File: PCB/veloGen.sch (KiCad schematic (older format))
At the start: 42 parts, among them J1 progButton, J2 Gen. IN, J3 Batt, P1 TTL_232R_3V3, P2 CONN_01X04, Q1 STL4P3LLH6, Q2 BSS138_ok, U1 ESP-WROOM-32, U2 TS1101, U3 TS1101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

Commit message: Added SEPIC ltspice model
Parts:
- gave numbers to parts that had none: 6
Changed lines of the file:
@@
 $EndComp
 $Comp
-L GND #PWR12
+L GND #PWR15
 U 1 1 58CDDA95
 P 6550 3600
-F 0 "#PWR12" H 6550 3350 50  0001 C CNN
+F 0 "#PWR15" H 6550 3350 50  0001 C CNN
 F 1 "GND" H 6555 3427 50  0000 C CNN
 F 2 "" H 6550 3600 50  0001 C CNN
@@
 NoConn ~ 10300 2600
 $Comp
-L +3V3 #PWR19
+L +3V3 #PWR22
 U 1 1 58CDF05C
 P 10600 2500
-F 0 "#PWR19" H 10600 2350 50  0001 C CNN
+F 0 "#PWR22" H 10600 2350 50  0001 C CNN
 F 1 "+3V3" H 10615 2673 50  0000 C CNN
 F 2 "" H 10600 2500 50  0001 C CNN
@@
 $EndComp
 $Comp
-L +BATT #PWR11
+L +BATT #PWR14
 U 1 1 58D0C801
 P 6550 2450
-F 0 "#PWR11" H 6550 2300 50  0001 C CNN
+F 0 "#PWR14" H 6550 2300 50  0001 C CNN
 F 1 "+BATT" H 6700 2550 50  0000 C CNN
 F 2 "" H 6550 2450 50  0001 C CNN
@@
 $EndComp
 $Comp
-L +3V3 #PWR13
+L +3V3 #PWR16
 U 1 1 58D133CF
 P 7050 2800
-F 0 "#PWR13" H 7050 2650 50  0001 C CNN
+F 0 "#PWR16" H 7050 2650 50  0001 C CNN
 F 1 "+3V3" V 7050 3050 50  0000 C CNN
 F 2 "" H 7050 2800 50  0001 C CNN
@@
 $EndComp
 $Comp
-L GND #PWR14
+L GND #PWR17
 U 1 1 58D1409D
 P 8050 2700
-F 0 "#PWR14" H 8050 2450 50  0001 C CNN
+F 0 "#PWR17" H 8050 2450 50  0001 C CNN
 F 1 "GND" V 8150 2650 50  0000 C CNN
 F 2 "" H 8050 2700 50  0001 C CNN
@@
 $EndComp
 $Comp
-L +3V3 #PWR5
+L +3V3 #PWR7
 U 1 1 58D16995
 P 3750 1250
-F 0 "#PWR5" H 3750 1100 50  0001 C CNN
+F 0 "#PWR7" H 3750 1100 50  0001 C CNN
 F 1 "+3V3" V 3750 1500 50  0000 C CNN
 F 2 "" H 3750 1250 50  0001 C CNN
@@
 $EndComp
 $Comp
-L GND #PWR7
+L GND #PWR9
 U 1 1 58D169A5
 P 4750 1150
-F 0 "#PWR7" H 4750 900 50  0001 C CNN
+F 0 "#PWR9" H 4750 900 50  0001 C CNN
 F 1 "GND" V 4750 950 50  0000 C CNN
 F 2 "" H 4750 1150 50  0001 C CNN
@@
 Igen
 $Comp
-L GND #PWR6
+L GND #PWR8
 U 1 1 58D1723C
 P 3800 1800
-F 0 "#PWR6" H 3800 1550 50  0001 C CNN
+F 0 "#PWR8" H 3800 1550 50  0001 C CNN
 F 1 "GND" H 3805 1627 50  0000 C CNN
 F 2 "" H 3800 1800 50  0001 C CNN
@@
 $EndComp
 $Comp
-L GND #PWR8
+L GND #PWR10
 U 1 1 58D18FFC
 P 4800 1800
-F 0 "#PWR8" H 4800 1550 50  0001 C CNN
+F 0 "#PWR10" H 4800 1550 50  0001 C CNN
 F 1 "GND" H 4805 1627 50  0000 C CNN
 F 2 "" H 4800 1800 50  0001 C CNN
@@
 buckPwm
 $Comp
-L +3V3 #PWR2
+L +3V3 #PWR4
 U 1 1 58D24DE5
 P 2550 5050
-F 0 "#PWR2" H 2550 4900 50  0001 C CNN
+F 0 "#PWR4" H 2550 4900 50  0001 C CNN
 F 1 "+3V3" H 2550 5200 50  0000 C CNN
 F 2 "" H 2550 5050 50  0001 C CNN
@@
 $EndComp
 $Comp
-L GND #PWR3
+L GND #PWR5
 U 1 1 58D25BFF
 P 2950 5100
-F 0 "#PWR3" H 2950 4850 50  0001 C CNN
+F 0 "#PWR5" H 2950 4850 50  0001 C CNN
 F 1 "GND" H 2950 5150 50  0000 C CNN
 F 2 "" H 2950 5100 50  0001 C CNN
@@
 $EndComp
 $Comp
-L GND #PWR9
+L GND #PWR12
 U 1 1 58D26A6B
 P 5050 5000
-F 0 "#PWR9" H 5050 4750 50  0001 C CNN
+F 0 "#PWR12" H 5050 4750 50  0001 C CNN
 F 1 "GND" H 5050 5050 50  0000 C CNN
 F 2 "" H 5050 5000 50  0001 C CNN
@@
 $EndComp
 $Comp
-L GND #PWR18
+L GND #PWR21
 U 1 1 58D236E7
 P 9950 4600
-F 0 "#PWR18" H 9950 4350 50  0001 C CNN
+F 0 "#PWR21" H 9950 4350 50  0001 C CNN
 F 1 "GND" H 9955 4427 50  0000 C CNN
 F 2 "" H 9950 4600 50  0001 C CNN
@@
 $EndComp
 $Comp
-L GND #PWR15
+L GND #PWR18
 U 1 1 58D25A85
 P 8750 5350
-F 0 "#PWR15" H 8750 5100 50  0001 C CNN
+F 0 "#PWR18" H 8750 5100 50  0001 C CNN
 F 1 "GND" V 8750 5150 50  0000 C CNN
 F 2 "" H 8750 5350 50  0001 C CNN
@@
 $EndComp
 $Comp
-L +3V3 #PWR16
+L +3V3 #PWR19
 U 1 1 58D1F535
 P 9100 4800
-F 0 "#PWR16" H 9100 4650 50  0001 C CNN
+F 0 "#PWR19" H 9100 4650 50  0001 C CNN
 F 1 "+3V3" H 9250 4850 50  0000 C CNN
 F 2 "" H 9100 4800 50  0001 C CNN
@@
 $EndComp
 $Comp
-L +3V3 #PWR17
+L +3V3 #PWR20
 U 1 1 58D1FFAD
 P 9300 5750
-F 0 "#PWR17" H 9300 5600 50  0001 C CNN
+F 0 "#PWR20" H 9300 5600 50  0001 C CNN
 F 1 "+3V3" H 9450 5800 50  0000 C CNN
 F 2 "" H 9300 5750 50  0001 C CNN
@@
 rstBtn
 $Comp
-L GND #PWR4
+L GND #PWR6
 U 1 1 58D25783
 P 3550 6800
-F 0 "#PWR4" H 3550 6550 50  0001 C CNN
+F 0 "#PWR6" H 3550 6550 50  0001 C CNN
 F 1 "GND" H 3400 6750 50  0000 C CNN
 F 2 "" H 3550 6800 50  0001 C CNN
@@
 $EndComp
 $Comp
-L GND #PWR10
+L GND #PWR13
 U 1 1 58D266BB
 P 5850 5850
-F 0 "#PWR10" H 5850 5600 50  0001 C CNN
+F 0 "#PWR13" H 5850 5600 50  0001 C CNN
 F 1 "GND" H 6150 5750 50  0000 C CNN
 F 2 "" H 5850 5850 50  0001 C CNN
@@
 NoConn ~ 5850 5700
 $Comp
-L GND #PWR1
+L GND #PWR11
 U 1 1 58D2F2FA
 P 4800 6750
-F 0 "#PWR1" H 4800 6500 50  0001 C CNN
+F 0 "#PWR11" H 4800 6500 50  0001 C CNN
 F 1 "GND" H 4850 6850 50  0000 C CNN
 F 2 "" H 4800 6750 50  0001 C CNN
@@
 $EndComp
 $Comp
-L R R?
+L R R14
 U 1 1 58E35502
 P 2200 6400
-F 0 "R?" V 1993 6400 50  0000 C CNN
+F 0 "R14" V 1993 6400 50  0000 C CNN
 F 1 "470R" V 2084 6400 50  0000 C CNN
 F 2 "" V 2130 6400 50  0001 C CNN
@@
 NoConn ~ 4900 5300
 $Comp
-L D_Zener D?
+L D_Zener D7
 U 1 1 58E3687C
 P 4050 3000
-F 0 "D?" V 4004 3079 50  0000 L CNN
+F 0 "D7" V 4004 3079 50  0000 L CNN
 F 1 "30V, 3W" V 4095 3079 50  0000 L CNN
 F 2 "" H 4050 3000 50  0001 C CNN
@@
 	8800 5150 8800 4300
 $Comp
-L Crystal Y?
+L Crystal Y1
 U 1 1 58E37985
 P 2200 5950
-F 0 "Y?" V 2000 5850 50  0000 L CNN
+F 0 "Y1" V 2000 5850 50  0000 L CNN
 F 1 "32.768 kHz" V 1900 5750 50  0000 L CNN
 F 2 "" H 2200 5950 50  0001 C CNN
@@
 	2400 5900 2400 6100
 $Comp
-L C C?
+L C C9
 U 1 1 58E3A322
 P 1850 5800
-F 0 "C?" V 1800 5700 50  0000 C CNN
+F 0 "C9" V 1800 5700 50  0000 C CNN
 F 1 "12pF" V 1689 5800 50  0000 C CNN
 F 2 "" H 1888 5650 50  0001 C CNN
@@
 $EndComp
 $Comp
-L C C?
+L C C12
 U 1 1 58E3A3E7
 P 1850 6100
-F 0 "C?" V 1900 6200 50  0000 C CNN
+F 0 "C12" V 1900 6200 50  0000 C CNN
 F 1 "12pF" V 1700 6100 50  0000 C CNN
 F 2 "" H 1888 5950 50  0001 C CNN
@@
 Connection ~ 2200 6100
 $Comp
-L GND #PWR?
+L GND #PWR3
 U 1 1 58E3C87D
 P 1650 6400
-F 0 "#PWR?" H 1650 6150 50  0001 C CNN
+F 0 "#PWR3" H 1650 6150 50  0001 C CNN
 F 1 "GND" V 1650 6200 50  0000 C CNN
 F 2 "" H 1650 6400 50  0001 C CNN
@@
 $EndComp
 $Comp
-L LED D?
+L LED D5
 U 1 1 58E350A9
 P 1850 6400
-F 0 "D?" H 2000 6300 50  0000 C CNN
+F 0 "D5" H 2000 6300 50  0000 C CNN
 F 1 "LED" H 1850 6300 50  0000 C CNN
 F 2 "LEDs:LED_0805" H 1850 6400 50  0001 C CNN
@@
 	2050 6400 2000 6400
 $Comp
-L GND #PWR?
+L GND #PWR2
 U 1 1 58E3DA98
 P 1650 6100
-F 0 "#PWR?" H 1650 5850 50  0001 C CNN
+F 0 "#PWR2" H 1650 5850 50  0001 C CNN
 F 1 "GND" V 1650 5900 50  0000 C CNN
 F 2 "" H 1650 6100 50  0001 C CNN
@@
 $EndComp
 $Comp
-L GND #PWR?
+L GND #PWR1
 U 1 1 58E3DB09
 P 1650 5800
-F 0 "#PWR?" H 1650 5550 50  0001 C CNN
+F 0 "#PWR1" H 1650 5550 50  0001 C CNN
 F 1 "GND" V 1650 5600 50  0000 C CNN
 F 2 "" H 1650 5800 50  0001 C CNN

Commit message: Schematic work
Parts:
- R3, R8: value R050 -> R010
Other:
- note added: "Gain = 100 x\n1 V / A"
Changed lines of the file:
@@
 P 3300 2500
 F 0 "R3" H 3370 2546 50  0000 L CNN
-F 1 "R050" H 3370 2455 50  0000 L CNN
+F 1 "R010" H 3370 2455 50  0000 L CNN
 F 2 "Resistors_SMD:R_0805" V 3230 2500 50  0001 C CNN
 F 3 "" H 3300 2500 50  0001 C CNN
@@
 P 6550 2800
 F 0 "R8" H 6620 2846 50  0000 L CNN
-F 1 "R050" H 6620 2755 50  0000 L CNN
+F 1 "R010" H 6620 2755 50  0000 L CNN
 F 2 "Resistors_SMD:R_0805" V 6480 2800 50  0001 C CNN
 F 3 "" H 6550 2800 50  0001 C CNN
@@
 Wire Wire Line
 	4800 6700 4800 6750
+Text Notes 4050 1950 0    60   ~ 0
+Gain = 100 x\n1 V / A
+Text Notes 7350 2350 0    60   ~ 0
+Gain = 100 x\n1 V / A
 $EndSCHEMATC

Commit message: Simplified schematic and started layout
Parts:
- removed C12, C9: 12pF, symbol C
- removed C3, C6: 470n, Capacitors_SMD:C_0805, symbol C
- removed C4, C7: 47n, Capacitors_SMD:C_0805, symbol C
- removed D7: 30V, 3W, symbol D_Zener
- removed J1: progButton, Pin_Headers:Pin_Header_Straight_1x02_Pitch2.54mm, symbol CONN_01X02
- removed R3, R8: R010, Resistors_SMD:R_0805, symbol R
- removed U2, U3: TS1101, TO_SOT_Packages_SMD:SOT-23-6_Handsoldering, symbol TS1101
- removed Y1: 32.768 kHz, symbol Crystal
- added U2: PROG, myStuff:EVQQ2, symbol TACTILE
- J3: value Batt -> Bat
- R14: footprint (none) -> Resistors_SMD:R_0805
- U4: footprint TO_SOT_Packages_SMD:SOT-23-6_Handsoldering -> TO_SOT_Packages_SMD:SOT-23-6
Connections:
- net labels added: sepicImax, sepicPwm
- net labels removed: Ibatt, IbattSign, Igen, buckPwm
- wire segments 134 -> 94
- no-connect marks 20 -> 25
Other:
- note removed: "Gain = 100 x\n1 V / A"
- moved on the sheet: C5, R6, R7

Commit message: completed an ugly pcb with minimalistic fuctionality
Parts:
- removed P1: TTL_232R_3V3, Pin_Headers:Pin_Header_Straight_1x06_Pitch2.54mm, symbol TTL_232R_3V3
- removed P2: CONN_01X04, Pin_Headers:Pin_Header_Straight_1x04_Pitch2.54mm, symbol CONN_01X04
- removed Q1: STL4P3LLH6, myStuff:PowerFLAT_2x2, symbol STL4P3LLH6
- removed Q2: BSS138_ok, TO_SOT_Packages_SMD:SOT-23, symbol BSS138_ok
- removed R10, R9: 200R, Resistors_SMD:R_0805, symbol R
- removed R11, R12: 4k7, Resistors_SMD:R_0805, symbol R
- removed R13: 4.7Meg, Resistors_SMD:R_0805, symbol R
- removed U2: PROG, myStuff:EVQQ2, symbol TACTILE
- added J1: Conn_01x06, myStuff:myPogoPads, symbol Conn_01x06
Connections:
- net labels added: progFlag
- wire segments 94 -> 75
- no-connect marks 25 -> 21
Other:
- note added: "5 V"
- note added: "GND"
- note added: "RXD"
- note added: "Rst"
- note added: "TXD"

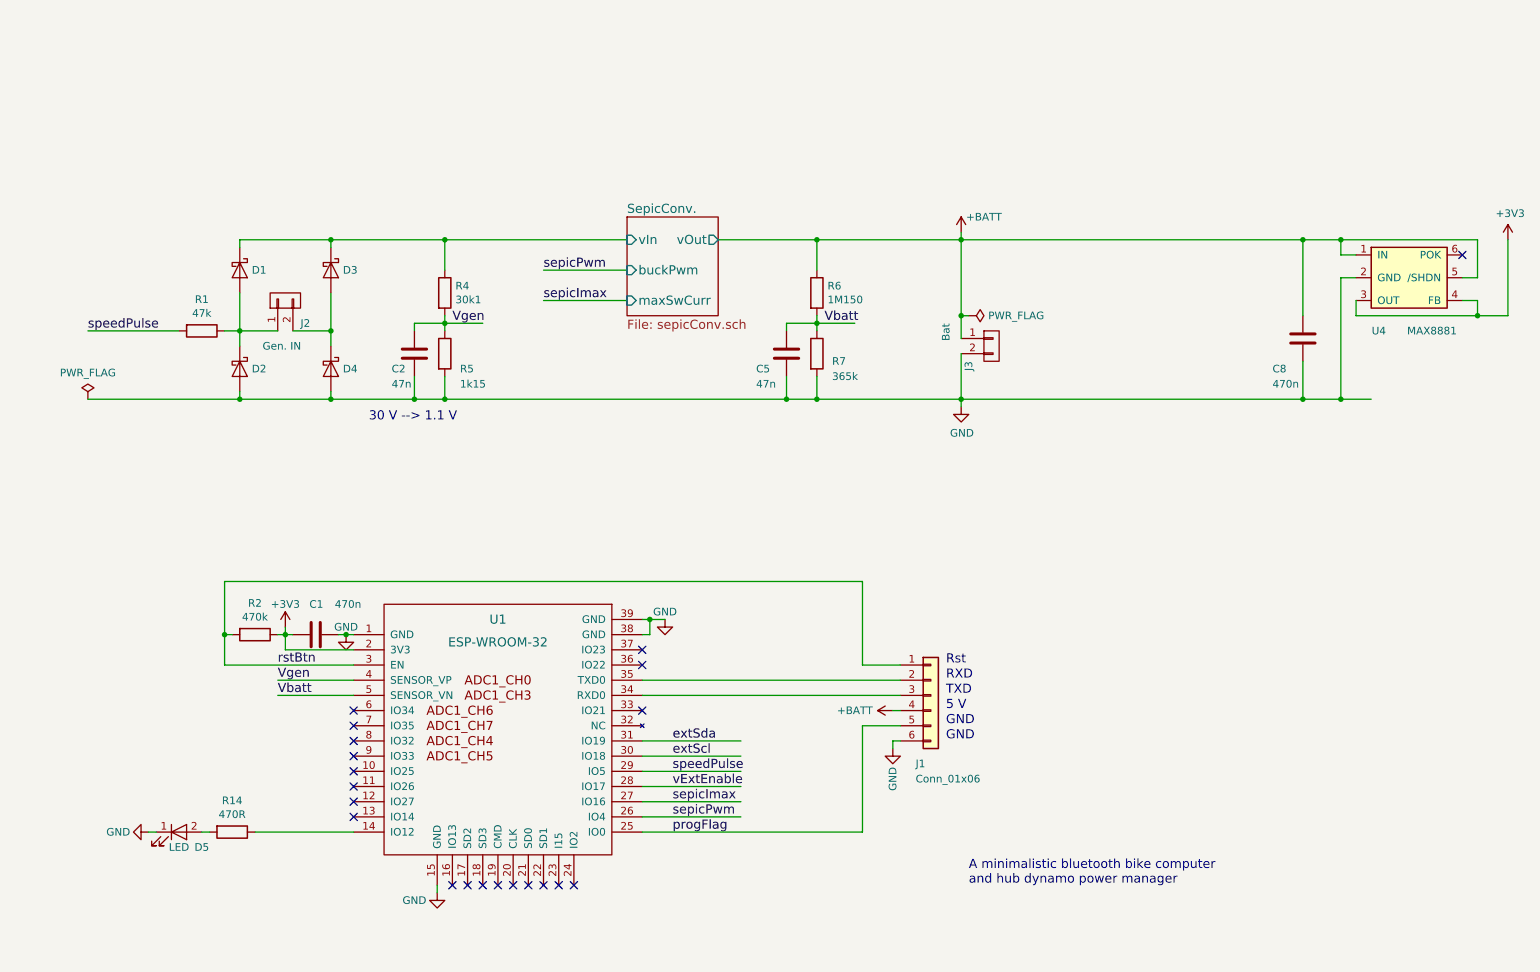
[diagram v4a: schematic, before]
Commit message: Added batery current sense
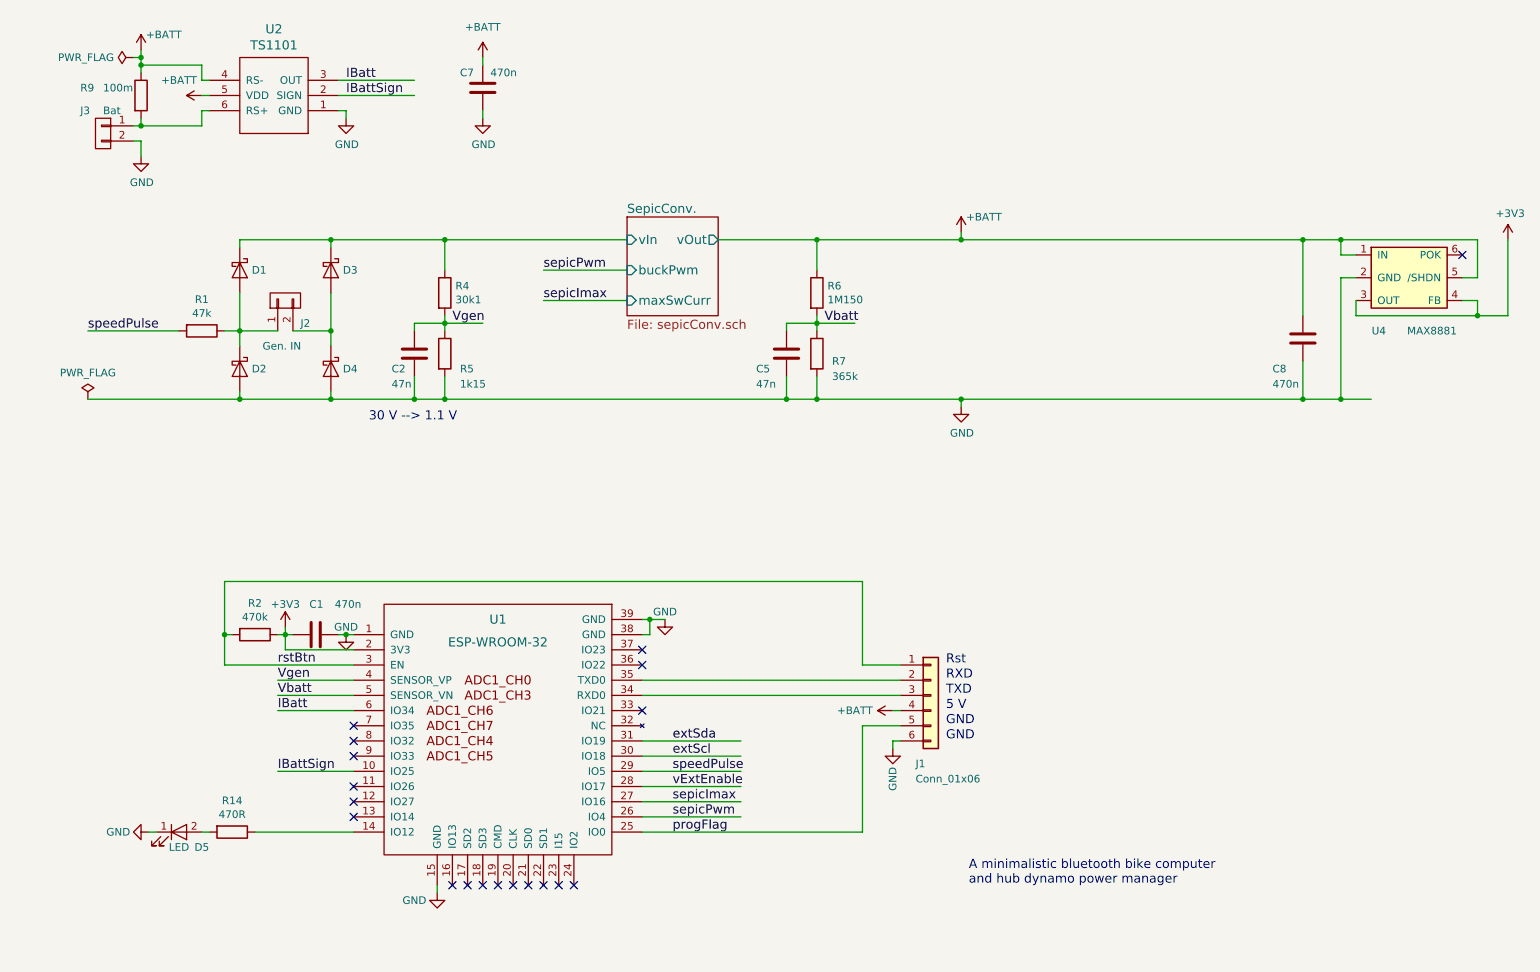
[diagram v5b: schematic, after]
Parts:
- added C7: 470n, Capacitors_SMD:C_0805, symbol C
- added R9: 100m, Resistors_SMD:R_1206, symbol R
- added U2: TS1101, TO_SOT_Packages_SMD:SOT-23-6_Handsoldering, symbol TS1101
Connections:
- net labels added: IBatt, IBattSign
- wire segments 75 -> 94
- no-connect marks 21 -> 19
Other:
- moved on the sheet: J3
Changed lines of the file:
@@
-EESchema Schematic File Version 2
+EESchema Schematic File Version 3
 LIBS:veloGen-rescue
 LIBS:power
@@
 Text Notes 3100 3700 0    60   ~ 0
 30 V --> 1.1 V
-NoConn ~ 3000 6000
 NoConn ~ 3000 6100
 NoConn ~ 3000 6200
@@
 Wire Wire Line
 	5400 2500 10400 2500
-Connection ~ 7000 2500
 Wire Wire Line
 	10400 2750 10300 2750
@@
 	6350 4750 2150 4750
 Connection ~ 2150 5100
-Wire Wire Line
-	7000 2450 7000 3150
 NoConn ~ 3000 5900
 NoConn ~ 3000 5800
@@
 L CONN_01X02 J3
 U 1 1 59D6FC9E
-P 7200 3200
-F 0 "J3" V 7050 3100 50  0000 R CNN
-F 1 "Bat" V 6900 3350 50  0000 R CNN
-F 2 "Pin_Headers:Pin_Header_Straight_1x02_Pitch2.54mm" H 7200 3200 50  0001 C CNN
-F 3 "" H 7200 3200 50  0001 C CNN
-	1    7200 3200
-	1    0    0    -1
-$EndComp
-Wire Wire Line
-	7000 3250 7000 3600
+P 1350 1800
+F 0 "J3" H 1500 1950 50  0000 R CNN
+F 1 "Bat" H 1350 1950 50  0000 R CNN
+F 2 "Pin_Headers:Pin_Header_Straight_1x02_Pitch2.54mm" H 1350 1800 50  0001 C CNN
+F 3 "" H 1350 1800 50  0001 C CNN
+	1    1350 1800
+	-1   0    0    -1
+$EndComp
+Wire Wire Line
+	1600 1850 1600 1950
 Connection ~ 7000 3550
-NoConn ~ 3000 5600
 NoConn ~ 3000 5700
 Text Label 5100 6200 0    60   ~ 0
@@
 L PWR_FLAG #FLG02
 U 1 1 59D79473
-P 7050 3000
-F 0 "#FLG02" H 7050 3075 50  0001 C CNN
-F 1 "PWR_FLAG" V 7050 3128 50  0000 L CNN
-F 2 "" H 7050 3000 50  0001 C CNN
-F 3 "" H 7050 3000 50  0001 C CNN
-	1    7050 3000
-	0    1    1    0
-$EndComp
-Wire Wire Line
-	7050 3000 7000 3000
-Connection ~ 7000 3000
+P 1550 1300
+F 0 "#FLG02" H 1550 1375 50  0001 C CNN
+F 1 "PWR_FLAG" V 1550 1428 50  0000 L CNN
+F 2 "" H 1550 1300 50  0001 C CNN
+F 3 "" H 1550 1300 50  0001 C CNN
+	1    1550 1300
+	0    -1   -1   0
+$EndComp
 Text Label 5100 6400 0    60   ~ 0
 progFlag
@@
 Wire Wire Line
 	6550 5800 6550 5850
+$Comp
+L TS1101 U2
+U 1 1 59D5A882
+P 2850 1450
+F 0 "U2" H 3225 1113 60  0000 C CNN
+F 1 "TS1101" H 3225 1219 60  0000 C CNN
+F 2 "TO_SOT_Packages_SMD:SOT-23-6_Handsoldering" H 3250 1050 60  0001 C CNN
+F 3 "https://www.silabs.com/documents/public/data-sheets/TS1100-01-02-03.pdf" H 4000 1200 60  0001 C CNN
+	1    2850 1450
+	-1   0    0    1
+$EndComp
+Wire Wire Line
+	7000 2450 7000 2500
+Connection ~ 7000 2500
+Wire Wire Line
+	7000 3600 7000 3550
+$Comp
+L GND #PWR011
+U 1 1 59D5B1BD
+P 1600 1950
+F 0 "#PWR011" H 1600 1700 50  0001 C CNN
+F 1 "GND" H 1605 1777 50  0000 C CNN
+F 2 "" H 1600 1950 50  0001 C CNN
+F 3 "" H 1600 1950 50  0001 C CNN
+	1    1600 1950
+	1    0    0    -1
+$EndComp
+Wire Wire Line
+	1550 1850 1600 1850
+$Comp
+L R R9
+U 1 1 59D5BCBC
+P 1600 1550
+F 0 "R9" H 1200 1600 50  0000 L CNN
+F 1 "100m" H 1350 1600 50  0000 L CNN
+F 2 "Resistors_SMD:R_1206" V 1530 1550 50  0001 C CNN
+F 3 "" H 1600 1550 50  0001 C CNN
+	1    1600 1550
+	1    0    0    -1
+$EndComp
+Wire Wire Line
+	1550 1750 2000 1750
+Wire Wire Line
+	1600 1750 1600 1700
+Wire Wire Line
+	2050 1650 2000 1650
+Wire Wire Line
+	2000 1650 2000 1750
+Connection ~ 1600 1750
+Wire Wire Line
+	1600 1250 1600 1400
+Wire Wire Line
+	1600 1350 2000 1350
+Wire Wire Line
+	2000 1350 2000 1450
+Wire Wire Line
+	2000 1450 2050 1450
+Wire Wire Line
+	1600 1300 1550 1300
+Connection ~ 1600 1350
+$Comp
+L +BATT #PWR02
+U 1 1 59D5CA8C
+P 1600 1250
+F 0 "#PWR02" H 1600 1100 50  0001 C CNN
+F 1 "+BATT" H 1750 1350 50  0000 C CNN
+F 2 "" H 1600 1250 50  0001 C CNN
+F 3 "" H 1600 1250 50  0001 C CNN
+	1    1600 1250
+	1    0    0    -1
+$EndComp
+Connection ~ 1600 1300
+Wire Wire Line
+	2000 1550 2050 1550
+$Comp
+L GND #PWR019
+U 1 1 59D5D9C8
+P 2950 1700
+F 0 "#PWR019" H 2950 1450 50  0001 C CNN
+F 1 "GND" H 2955 1527 50  0000 C CNN
+F 2 "" H 2950 1700 50  0001 C CNN
+F 3 "" H 2950 1700 50  0001 C CNN
+	1    2950 1700
+	1    0    0    -1
+$EndComp
+Wire Wire Line
+	2900 1650 2950 1650
+Wire Wire Line
+	2950 1650 2950 1700
+Wire Wire Line
+	2900 1450 3400 1450
+Wire Wire Line
+	2900 1550 3400 1550
+Wire Wire Line
+	3000 5600 2500 5600
+Text Label 2500 5600 0    60   ~ 0
+IBatt
+Wire Wire Line
+	3000 6000 2500 6000
+Text Label 2500 6000 0    60   ~ 0
+IBattSign
+Text Label 2950 1450 0    60   ~ 0
+IBatt
+Text Label 2950 1550 0    60   ~ 0
+IBattSign
+$Comp
+L C C7
+U 1 1 59D5F134
+P 3850 1500
+F 0 "C7" H 3700 1600 50  0000 L CNN
+F 1 "470n" H 3900 1600 50  0000 L CNN
+F 2 "Capacitors_SMD:C_0805" H 3888 1350 50  0001 C CNN
+F 3 "" H 3850 1500 50  0001 C CNN
+	1    3850 1500
+	1    0    0    -1
+$EndComp
+Wire Wire Line
+	3850 1300 3850 1350
+$Comp
+L GND #PWR021
+U 1 1 59D5F40C
+P 3850 1700
+F 0 "#PWR021" H 3850 1450 50  0001 C CNN
+F 1 "GND" H 3855 1527 50  0000 C CNN
+F 2 "" H 3850 1700 50  0001 C CNN
+F 3 "" H 3850 1700 50  0001 C CNN
+	1    3850 1700
+	1    0    0    -1
+$EndComp
+Wire Wire Line
+	3850 1700 3850 1650
+$Comp
+L +BATT #PWR?
+U 1 1 59D607AF
+P 2000 1550
+F 0 "#PWR?" H 2000 1400 50  0001 C CNN
+F 1 "+BATT" V 2100 1700 50  0000 C CNN
+F 2 "" H 2000 1550 50  0001 C CNN
+F 3 "" H 2000 1550 50  0001 C CNN
+	1    2000 1550
+	0    -1   -1   0
+$EndComp
+$Comp
+L +BATT #PWR?
+U 1 1 59D60AAD
+P 3850 1300
+F 0 "#PWR?" H 3850 1150 50  0001 C CNN
+F 1 "+BATT" H 3850 1500 50  0000 C CNN
+F 2 "" H 3850 1300 50  0001 C CNN
+F 3 "" H 3850 1300 50  0001 C CNN
+	1    3850 1300
+	1    0    0    -1
+$EndComp
 $EndSCHEMATC
